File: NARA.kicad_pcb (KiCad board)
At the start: 2 copper layers, 42.4 x 93.9 mm, 0 parts

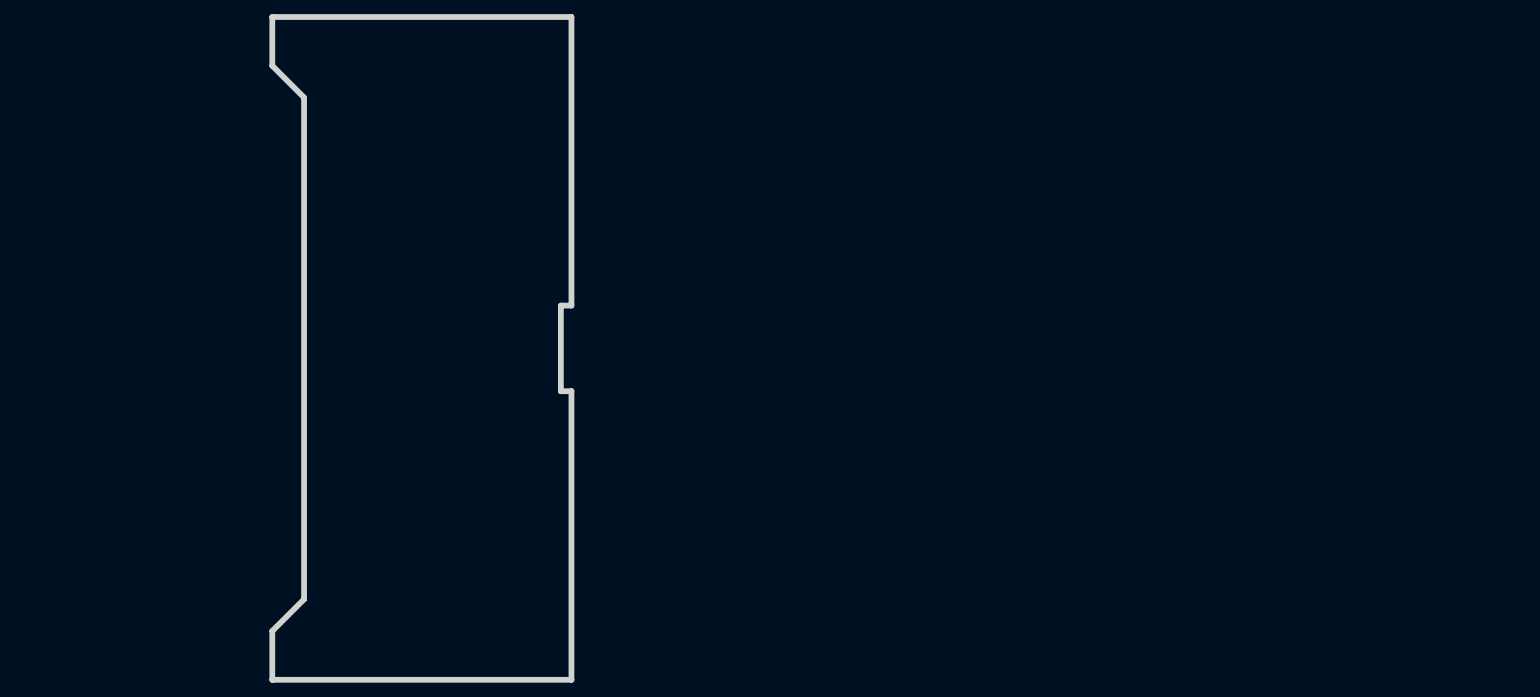
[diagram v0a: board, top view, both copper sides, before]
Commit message: Update footprints, prepare to place composants
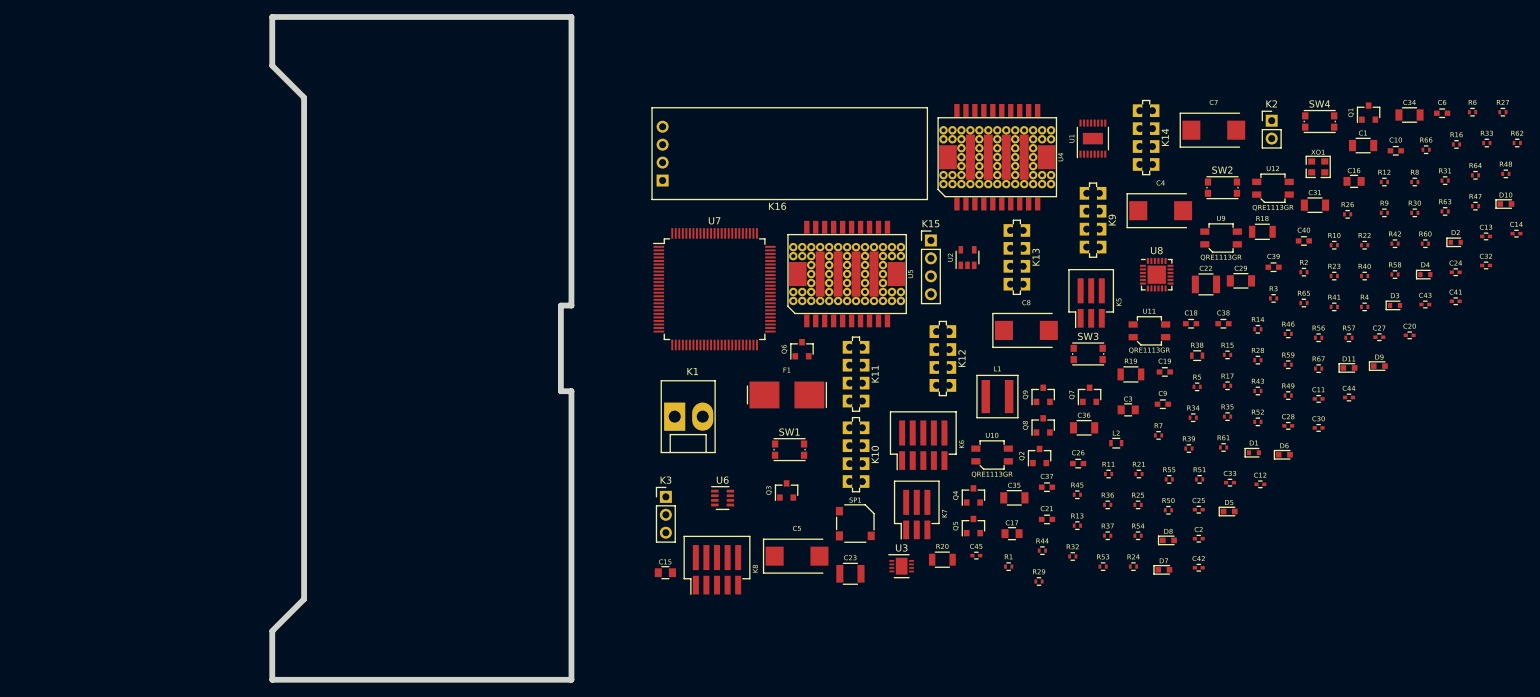
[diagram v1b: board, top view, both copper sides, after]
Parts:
- added C1: C_0038, DVB_Capacitors_Ceramic:C_1206, F.Cu at (239.6, 69.8)
- added C10: C_0033, DVB_Capacitors_Ceramic:C_0603, F.Cu at (244.2, 70.5)
- added C11: C_0002, DVB_Capacitors_Ceramic:C_0402, F.Cu at (233.3, 105.7)
- added C12: C_0034, DVB_Capacitors_Ceramic:C_0402, F.Cu at (225.0, 117.8)
- added C13: C_0034, DVB_Capacitors_Ceramic:C_0402, F.Cu at (257.0, 82.6)
- added C14: C_0045, DVB_Capacitors_Ceramic:C_0402, F.Cu at (261.3, 82.2)
- added C15: C_0056, DVB_Capacitors_Ceramic:C_0805, F.Cu at (140.7, 130.3)
- added C16: C_0056, DVB_Capacitors_Ceramic:C_0805, F.Cu at (238.3, 74.8)
- added C17: C_0056, DVB_Capacitors_Ceramic:C_0805, F.Cu at (189.8, 124.7)
- added C18: C_220nF, DVB_Capacitors_Ceramic:C_0603, F.Cu at (215.2, 95.0)
- added C19: C_220nF, DVB_Capacitors_Ceramic:C_0603, F.Cu at (211.5, 101.8)
- added C2: C_0001, DVB_Capacitors_Ceramic:C_0402, F.Cu at (216.3, 125.5)
- added C20: C_0001, DVB_Capacitors_Ceramic:C_0402, F.Cu at (246.2, 96.7)
- added C21: C_0033, DVB_Capacitors_Ceramic:C_0603, F.Cu at (194.8, 122.7)
- added C22: C_0040, DVB_Capacitors_Ceramic:C_1210, F.Cu at (217.3, 89.4)
- added C23: C_0040, DVB_Capacitors_Ceramic:C_1210, F.Cu at (166.9, 130.4)
- added C24: C_0002, DVB_Capacitors_Ceramic:C_0402, F.Cu at (252.7, 87.7)
- added C25: C_0001, DVB_Capacitors_Ceramic:C_0402, F.Cu at (216.3, 121.3)
- added C26: C_0037, DVB_Capacitors_Ceramic:C_0603, F.Cu at (199.2, 114.8)
- added C27: C_0043, DVB_Capacitors_Ceramic:C_0402, F.Cu at (241.9, 96.9)
- added C28: C_0002, DVB_Capacitors_Ceramic:C_0402, F.Cu at (229.0, 109.5)
- added C29: C_0007, DVB_Capacitors_Ceramic:C_1206, F.Cu at (222.2, 88.9)
- added C3: C_0056, DVB_Capacitors_Ceramic:C_0805, F.Cu at (206.3, 107.2)
- added C30: C_0045, DVB_Capacitors_Ceramic:C_0402, F.Cu at (233.3, 109.8)
- added C31: C_0007, DVB_Capacitors_Ceramic:C_1206, F.Cu at (232.7, 78.2)
- added C32: C_0043, DVB_Capacitors_Ceramic:C_0402, F.Cu at (257.0, 86.8)
- added C33: C_0045, DVB_Capacitors_Ceramic:C_0402, F.Cu at (220.7, 117.5)
- added C34: C_0007, DVB_Capacitors_Ceramic:C_1206, F.Cu at (246.1, 65.4)
- added C35: C_0007, DVB_Capacitors_Ceramic:C_1206, F.Cu at (190.2, 119.7)
- added C36: C_0007, DVB_Capacitors_Ceramic:C_1206, F.Cu at (200.0, 109.7)
- added C37: C_0037, DVB_Capacitors_Ceramic:C_0603, F.Cu at (194.8, 118.2)
- added C38: C_0037, DVB_Capacitors_Ceramic:C_0603, F.Cu at (219.8, 95.0)
- added C39: C_0037, DVB_Capacitors_Ceramic:C_0603, F.Cu at (226.9, 87.0)
- added C4: C_47uF, DVB_Capacitors_Tantalum:CP_EIA-7343-31, F.Cu at (210.9, 79.0)
- added C40: C_0037, DVB_Capacitors_Ceramic:C_0603, F.Cu at (231.2, 83.3)
- added C41: C_0001, DVB_Capacitors_Ceramic:C_0402, F.Cu at (252.7, 91.8)
- added C42: C_0045, DVB_Capacitors_Ceramic:C_0402, F.Cu at (216.3, 129.6)
- added C43: C_0002, DVB_Capacitors_Ceramic:C_0402, F.Cu at (248.4, 92.3)
- added C44: C_0002, DVB_Capacitors_Ceramic:C_0402, F.Cu at (237.6, 105.5)
- added C45: C_470nF, DVB_Capacitors_Ceramic:C_0402, F.Cu at (184.8, 127.8)
- added C5: C_47uF, DVB_Capacitors_Tantalum:CP_EIA-7343-31, F.Cu at (159.4, 127.9)
- added C6: C_0037, DVB_Capacitors_Ceramic:C_0603, F.Cu at (250.8, 65.2)
- added C7: C_47uF, DVB_Capacitors_Tantalum:CP_EIA-7343-31, F.Cu at (218.4, 67.6)
- added C8: C_47uF, DVB_Capacitors_Tantalum:CP_EIA-7343-31, F.Cu at (191.9, 96.0)
- added C9: C_0033, DVB_Capacitors_Ceramic:C_0603, F.Cu at (211.2, 106.4)
- added D1: D_0022, DVB_Diodes:D_SOD-523, F.Cu at (224.1, 113.3)
- added D10: D_0001, DVB_LED:LED_0603-red, F.Cu at (259.8, 78.1)
- added D11: D_0001, DVB_LED:LED_0603-red, F.Cu at (237.6, 101.3)
- added D2: D_0022, DVB_Diodes:D_SOD-523, F.Cu at (252.7, 83.5)
- added D3: D_0022, DVB_Diodes:D_SOD-523, F.Cu at (244.1, 92.4)
- added D4: D_0022, DVB_Diodes:D_SOD-523, F.Cu at (248.4, 88.0)
- added D5: D_0001, DVB_LED:LED_0603-red, F.Cu at (220.6, 121.6)
- added D6: D_0001, DVB_LED:LED_0603-red, F.Cu at (228.4, 113.6)
- added D7: D_0001, DVB_LED:LED_0603-red, F.Cu at (211.3, 129.9)
- added D8: D_0001, DVB_LED:LED_0603-red, F.Cu at (212.0, 125.7)
- added D9: D_0001, DVB_LED:LED_0603-red, F.Cu at (241.9, 101.0)
- added F1: F_001, DVB_F:F-OMNI-BLOCK, F.Cu at (157.9, 105.1)
- added K1: K_KK-41791-02, Connectors_Molex:Molex_KK-41791-02_02x3.96mm_Straight, F.Cu at (142.1, 108.2)
- added K10: TOF_LD, NARA_Lib:GYVL53L0X, F.Cu at (167.7, 113.6)
- added K11: TOF_LS, NARA_Lib:GYVL53L0X, F.Cu at (167.7, 102.2)
- added K12: TOF_LR, NARA_Lib:GYVL53L0X, F.Cu at (180.0, 99.9)
- added K13: TOF_RD, NARA_Lib:GYVL53L0X, F.Cu at (190.5, 85.6)
- added K14: TOF_RS, NARA_Lib:GYVL53L0X, F.Cu at (208.8, 68.6)
- added K15: UART, Pin_Headers:Pin_Header_Straight_1x04_Pitch2.54mm, F.Cu at (178.3, 83.2)
- added K16: OLED_128x32, NARA_Lib:OLED_128x32, F.Cu at (156.6, 69.4)
- added K2: PW_MOT, Pin_Headers:Pin_Header_Straight_1x02_Pitch2.54mm, F.Cu at (226.6, 66.2)
- added K3: PROG, Pin_Headers:Pin_Header_Straight_1x03_Pitch2.54mm, F.Cu at (140.8, 119.5)
- added K5: K_PicoSPOX-3, NARA_Lib:K_PicoSPOX-3, F.Cu at (201.0, 90.6)
- added K6: K_0002, DVB_Connectors:K_PicoSPOX-5, F.Cu at (177.3, 110.7)
- added K7: K_PicoSPOX-3, NARA_Lib:K_PicoSPOX-3, F.Cu at (176.3, 120.6)
- added K8: K_0002, DVB_Connectors:K_PicoSPOX-5, F.Cu at (148.0, 128.4)
- added K9: TOF_LF, NARA_Lib:GYVL53L0X, F.Cu at (201.3, 80.3)
- added L1: L_0002, DVB_Inductors:L_5030-Coilcraft, F.Cu at (187.8, 105.3)
- added L2: L_0010, DVB_Inductors:L_0603, F.Cu at (204.6, 111.9)
- added Q1: Q_0004, DVB_SOT:SOT_23, F.Cu at (240.3, 65.1)
- added Q2: Q_0007, DVB_SOT:SOT_23, F.Cu at (193.7, 113.7)
- added Q3: Q_0007, DVB_SOT:SOT_23, F.Cu at (157.9, 118.6)
- added Q4: Q_0007, DVB_SOT:SOT_23, F.Cu at (184.4, 119.3)
- added Q5: Q_0007, DVB_SOT:SOT_23, F.Cu at (184.4, 123.7)
- added Q6: Q_0007, DVB_SOT:SOT_23, F.Cu at (160.1, 98.6)
- added Q7: Q_0007, DVB_SOT:SOT_23, F.Cu at (200.8, 105.1)
- added Q8: Q_0004, DVB_SOT:SOT_23, F.Cu at (194.2, 109.4)
- added Q9: Q_0004, DVB_SOT:SOT_23, F.Cu at (194.2, 105.1)
- added R1: R_0002, DVB_Resistors:R_0402, F.Cu at (189.4, 129.4)
- added R10: R_0002, DVB_Resistors:R_0402, F.Cu at (235.5, 83.9)
- added R11: R_0111, DVB_Resistors:R_0402, F.Cu at (203.5, 116.3)
- added R12: R_0002, DVB_Resistors:R_0402, F.Cu at (242.6, 74.9)
- added R13: R_0002, DVB_Resistors:R_0402, F.Cu at (199.1, 123.6)
- added R14: R_0111, DVB_Resistors:R_0402, F.Cu at (224.7, 95.8)
- added R15: R_0002, DVB_Resistors:R_0402, F.Cu at (220.4, 99.4)
- added R16: R_0002, DVB_Resistors:R_0402, F.Cu at (252.8, 69.6)
- added R17: R_0030, DVB_Resistors:R_0402, F.Cu at (220.4, 103.8)
- added R18: R_0088, DVB_Resistors:R_1206, F.Cu at (225.3, 82.0)
- added R19: R_0093, DVB_Resistors:R_1206, F.Cu at (206.7, 102.2)
- added R2: R_0002, DVB_Resistors:R_0402, F.Cu at (231.2, 87.7)
- added R20: R_0093, DVB_Resistors:R_1206, F.Cu at (180.0, 128.4)
- added R21: R_0015, DVB_Resistors:R_0402, F.Cu at (207.8, 116.3)
- added R22: R_0015, DVB_Resistors:R_0402, F.Cu at (239.8, 83.9)
- added R23: R_0118, DVB_Resistors:R_0402, F.Cu at (235.5, 88.3)
- added R24: R_0015, DVB_Resistors:R_0402, F.Cu at (207.0, 129.4)
- added R25: R_0104, DVB_Resistors:R_0402, F.Cu at (207.7, 120.7)
- added R26: R_0104, DVB_Resistors:R_0402, F.Cu at (237.4, 79.5)
- added R27: R_0104, DVB_Resistors:R_0402, F.Cu at (259.4, 65.0)
- added R28: R_0104, DVB_Resistors:R_0402, F.Cu at (224.7, 100.2)
- added R29: R_0105, DVB_Resistors:R_0402, F.Cu at (193.7, 131.5)
- added R3: R_0002, DVB_Resistors:R_0402, F.Cu at (226.9, 91.4)
- added R30: R_0105, DVB_Resistors:R_0402, F.Cu at (246.9, 79.3)
- added R31: R_0015, DVB_Resistors:R_0402, F.Cu at (251.2, 74.7)
- added R32: R_0015, DVB_Resistors:R_0402, F.Cu at (198.4, 128.0)
- added R33: R_0015, DVB_Resistors:R_0402, F.Cu at (257.1, 69.4)
- added R34: R_0015, DVB_Resistors:R_0402, F.Cu at (215.5, 108.3)
- added R35: R_0015, DVB_Resistors:R_0402, F.Cu at (220.4, 108.2)
- added R36: R_0015, DVB_Resistors:R_0402, F.Cu at (203.4, 120.7)
- added R37: R_0002, DVB_Resistors:R_0402, F.Cu at (203.4, 125.0)
- added R38: R_0076, DVB_Resistors:R_0603, F.Cu at (216.1, 99.5)
- added R39: R_0002, DVB_Resistors:R_0402, F.Cu at (214.9, 112.7)
- added R4: R_0002, DVB_Resistors:R_0402, F.Cu at (239.8, 92.6)
- added R40: R_0002, DVB_Resistors:R_0402, F.Cu at (239.8, 88.3)
- added R41: R_0002, DVB_Resistors:R_0402, F.Cu at (235.5, 92.6)
- added R42: R_0002, DVB_Resistors:R_0402, F.Cu at (244.1, 83.7)
- added R43: R_0002, DVB_Resistors:R_0402, F.Cu at (224.7, 104.5)
- added R44: R_0002, DVB_Resistors:R_0402, F.Cu at (194.1, 127.1)
- added R45: R_0002, DVB_Resistors:R_0402, F.Cu at (199.1, 119.2)
- added R46: R_0002, DVB_Resistors:R_0402, F.Cu at (229.0, 96.4)
- added R47: R_0033, DVB_Resistors:R_0402, F.Cu at (255.5, 78.4)
- added R48: R_0033, DVB_Resistors:R_0402, F.Cu at (259.8, 73.8)
- added R49: R_0033, DVB_Resistors:R_0402, F.Cu at (229.0, 105.2)
- added R5: R_0002, DVB_Resistors:R_0402, F.Cu at (216.1, 103.9)
- added R50: R_0033, DVB_Resistors:R_0402, F.Cu at (212.0, 121.4)
- added R51: R_0003, DVB_Resistors:R_0402, F.Cu at (216.4, 117.1)
- added R52: R_0003, DVB_Resistors:R_0402, F.Cu at (224.7, 108.9)
- added R53: R_0105, DVB_Resistors:R_0402, F.Cu at (202.7, 129.4)
- added R54: R_0105, DVB_Resistors:R_0402, F.Cu at (207.7, 125.0)
- added R55: R_0105, DVB_Resistors:R_0402, F.Cu at (212.1, 117.1)
- added R56: R_0105, DVB_Resistors:R_0402, F.Cu at (233.3, 97.0)
- added R57: R_0104, DVB_Resistors:R_0402, F.Cu at (237.6, 97.0)
- added R58: R_0033, DVB_Resistors:R_0402, F.Cu at (244.1, 88.0)
- added R59: R_0105, DVB_Resistors:R_0402, F.Cu at (229.0, 100.8)
- added R6: R_0002, DVB_Resistors:R_0402, F.Cu at (255.1, 65.0)
- added R60: R_0105, DVB_Resistors:R_0402, F.Cu at (248.4, 83.7)
- added R61: R_0033, DVB_Resistors:R_0402, F.Cu at (219.8, 112.5)
- added R62: R_0111, DVB_Resistors:R_0402, F.Cu at (261.4, 69.4)
- added R63: R_0111, DVB_Resistors:R_0402, F.Cu at (251.2, 79.1)
- added R64: R_0111, DVB_Resistors:R_0402, F.Cu at (255.5, 74.0)
- added R65: R_0111, DVB_Resistors:R_0402, F.Cu at (231.2, 92.1)
- added R66: R_0111, DVB_Resistors:R_0402, F.Cu at (248.5, 70.4)
- added R67: R_0111, DVB_Resistors:R_0402, F.Cu at (233.3, 101.4)
- added R7: R_0111, DVB_Resistors:R_0402, F.Cu at (210.6, 110.8)
- added R8: R_0002, DVB_Resistors:R_0402, F.Cu at (246.9, 74.9)
- added R9: R_0002, DVB_Resistors:R_0402, F.Cu at (242.6, 79.3)
- added SP1: SP_0001, DVB_Buzzers:SP_KSSG-5x5x3, F.Cu at (167.6, 123.3)
- added SW1: SW_KMR2, Buttons_Switches_SMD:SW_SPST_KMR2, F.Cu at (158.3, 112.8)
- added SW2: SW_KMR2, Buttons_Switches_SMD:SW_SPST_KMR2, F.Cu at (219.6, 75.7)
- added SW3: SW_KMR2, Buttons_Switches_SMD:SW_SPST_KMR2, F.Cu at (200.6, 99.3)
- added SW4: SW_KMR2, Buttons_Switches_SMD:SW_SPST_KMR2, F.Cu at (233.4, 66.4)
- added U1: U_LT8610ABIMSE-3.3, DVB_SSOP:MSOP_16-1EP_3x4_P0.5, F.Cu at (201.3, 68.8)
- added U10: QRE1113GR, NARA_Lib:QRE1113GR, F.Cu at (187.0, 113.6)
- added U11: QRE1113GR, NARA_Lib:QRE1113GR, F.Cu at (209.3, 96.0)
- added U12: QRE1113GR, NARA_Lib:QRE1113GR, F.Cu at (226.8, 75.8)
- added U2: U_AP2204K-5.0TRG1, DVB_SOT:SOT_23-5, F.Cu at (183.5, 85.6)
- added U3: LTC2944, Housings_DFN_QFN:DFN-8-1EP_3x3mm_Pitch0.5mm, F.Cu at (174.2, 129.3)
- added U4: L6234, NARA_Lib:PowerSO-20, F.Cu at (187.7, 71.4)
- added U5: L6234, NARA_Lib:PowerSO-20, F.Cu at (166.5, 88.0)
- added U6: LTC2955TS8-1, TO_SOT_Packages_SMD:SOT-23-8, F.Cu at (148.8, 119.7)
- added U7: STM32H743VITx, Housings_QFP:LQFP-100_14x14mm_Pitch0.5mm, F.Cu at (147.7, 90.1)
- added U8: ICM-20689, Housings_DFN_QFN:QFN-24-1EP_4x4mm_Pitch0.5mm, F.Cu at (210.3, 88.1)
- added U9: QRE1113GR, NARA_Lib:QRE1113GR, F.Cu at (219.4, 82.9)
- added XO1: XO_8Z-16, DVB_Clock:XO_8Z, F.Cu at (233.2, 72.8)

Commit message: First components placement, Autoroute in progress
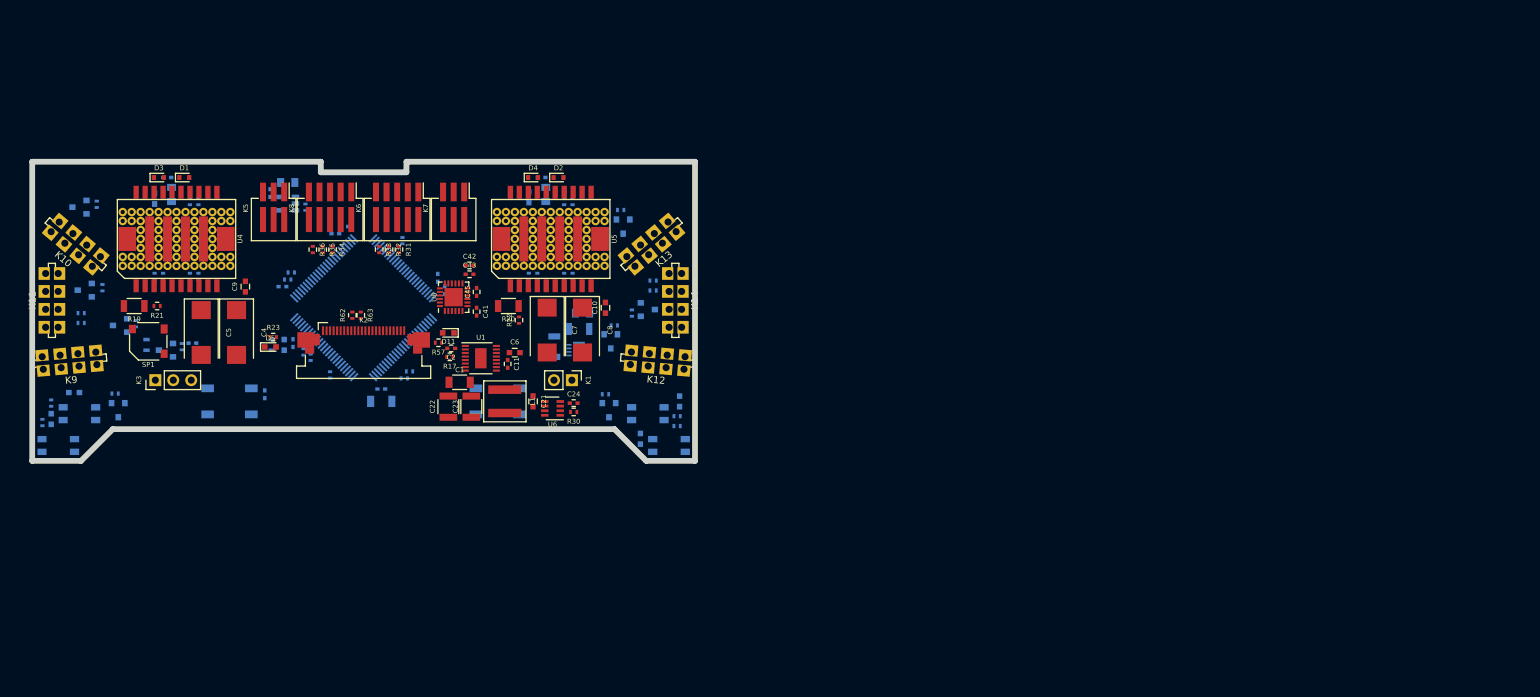
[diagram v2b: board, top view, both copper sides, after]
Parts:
- removed C20: C_0001, DVB_Capacitors_Ceramic:C_0402
- removed C27, C32: C_0043, DVB_Capacitors_Ceramic:C_0402
- removed D10, D6, D7, D8, D9: D_0001, DVB_LED:LED_0603-red
- removed K15: UART, Pin_Headers:Pin_Header_Straight_1x04_Pitch2.54mm
- removed K16: OLED_128x32, NARA_Lib:OLED_128x32
- removed R24: R_0015, DVB_Resistors:R_0402
- removed R25, R26, R27, R28: R_0104, DVB_Resistors:R_0402
- removed R51, R52: R_0003, DVB_Resistors:R_0402
- removed R58, R61: R_0033, DVB_Resistors:R_0402
- removed R59, R60: R_0105, DVB_Resistors:R_0402
- removed SW3, SW4: SW_KMR2, Buttons_Switches_SMD:SW_SPST_KMR2
- removed XO1: XO_8Z-16, DVB_Clock:XO_8Z
- C12, C13, C14, C15, C16, C17, C18, C19, C25, C26, C28, C29, C3, C30, C33, C37, C38, C39, C40, C44, L2, Q1, Q2, Q3, Q4, Q5, Q6, Q7, Q8, Q9, R1, R10, R11, R12, R13, R14, R15, R16, R18, R2, R29, R3, R37, R38, R39, R4, R40, R41, R42, R43, R44, R45, R46, R47, R48, R49, R5, R50, R53, R54, R55, R56, R6, R64, R65, R66, R67, R7, R8, R9, U10, U11, U12, U2, U9: moved to B.Cu
- C31, C34, C35, C36: value C_0007 -> C_0002; footprint DVB_Capacitors_Ceramic:C_1206 -> DVB_Capacitors_Ceramic:C_0402; moved to B.Cu
- F1: value F_001 -> FUSE; footprint DVB_F:F-OMNI-BLOCK -> DVB_F:F_1206; moved to B.Cu
- K1: value K_KK-41791-02 -> BATT; footprint Connectors_Molex:Molex_KK-41791-02_02x3.96mm_Straight -> DVB_Connectors:Pin_Header_Straight_1x02_Pitch2.54mm
- K12: value TOF_LR -> TOF_RF
- K2: value PW_MOT -> K_FPC_52435-2471; footprint Pin_Headers:Pin_Header_Straight_1x02_Pitch2.54mm -> DVB_Connectors:K_FPC_52435-2471
- K3: footprint Pin_Headers:Pin_Header_Straight_1x03_Pitch2.54mm -> DVB_Connectors:Pin_Header_Straight_1x03_Pitch2.54mm
- SW1, SW2: value SW_KMR2 -> SW_SKQG; footprint Buttons_Switches_SMD:SW_SPST_KMR2 -> DVB_Buttons:SPST_SKQG; moved to B.Cu
- U3: footprint Housings_DFN_QFN:DFN-8-1EP_3x3mm_Pitch0.5mm -> DVB_QFN_DFN:DFN_8-1EP_3x3mm_P0.5mm; moved to B.Cu
- U6: footprint TO_SOT_Packages_SMD:SOT-23-8 -> DVB_SOT:SOT_23-8
- U7: footprint Housings_QFP:LQFP-100_14x14mm_Pitch0.5mm -> DVB_QFP:LQFP-100_14x14mm_Pitch0.5mm; moved to B.Cu
- U8: footprint Housings_DFN_QFN:QFN-24-1EP_4x4mm_Pitch0.5mm -> DVB_QFN_DFN:QFN-24-1EP_4x4mm_Pitch0.5mm
- moved R48 208.6 mm to (53.8, 106.2), turned to 90 degrees
- moved R47 205.3 mm to (52.5, 109.0), turned to 270 degrees
- moved R64 198.6 mm to (58.0, 94.9)
- moved R40 179.9 mm to (60.2, 78.1), turned to 90 degrees
- moved C14 176.6 mm to (84.8, 76.5), turned to 90 degrees
- moved D3 176.0 mm to (69.0, 74.3)
- moved R12 174.7 mm to (68.4, 88.3), turned to 270 degrees
- moved R41 174.5 mm to (61.0, 89.9), turned to 90 degrees
- moved Q1 173.6 mm to (70.0, 98.8), turned to 270 degrees
- moved R65 173.2 mm to (58.0, 93.5), turned to 180 degrees
- moved R9 168.2 mm to (74.6, 88.3), turned to 270 degrees
- moved U9 167.3 mm to (54.8, 112.2)
- moved R62 166.8 mm to (96.4, 93.8), turned to 90 degrees
- moved C38 163.1 mm to (57.0, 104.8), turned to 180 degrees
- moved C12 160.8 mm to (70.2, 74.3)
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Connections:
- C10 pad 1: +HBAT -> +BATT
- C21 pad 1: +BATT -> GND
- C21 pad 2: GND -> +BATT
- C4 pad 1: +HBAT -> +BATT
- C5 pad 1: +HBAT -> +BATT
- C7 pad 1: +HBAT -> +BATT
- C8 pad 1: +HBAT -> +BATT
- C9 pad 1: +HBAT -> +BATT
- D1 pad 2: +HBAT -> +BATT
- D2 pad 2: +HBAT -> +BATT
- K2 pad 1: +BATT -> GND
- K2 pad 2: +HBAT -> /SW_PW
- SW1 pad 1: GND -> /SW_PW
- SW1 pad 2: Net-(SW1-Pad2) -> GND
- U4 pad 12: +HBAT -> +BATT
- U4 pad 9: +HBAT -> +BATT
- U5 pad 12: +HBAT -> +BATT
- U5 pad 9: +HBAT -> +BATT
- U6 pad 5: Net-(SW1-Pad2) -> /SW_PW
- U7 pad 12: Net-(C27-Pad2) -> (no net)
- U7 pad 13: Net-(C32-Pad1) -> (no net)
- U7 pad 17: (no net) -> /EXT_ADC1
- U7 pad 18: (no net) -> /EXT_ADC2
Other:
- board size 42.4 x 93.9 mm -> 93.9 x 42.4 mm
- net class Default: clearance 0.2 -> 0.13; trace_width 0.25 -> 0.13; via_drill 0.4 -> 0.2
- rule trace_clearance: 0.2 -> 0.13
- rule trace_min: 0.2 -> 0.125
- rule via_min_drill: 0.3 -> 0.2
- rule via_min_size: 0.4 -> 0.6

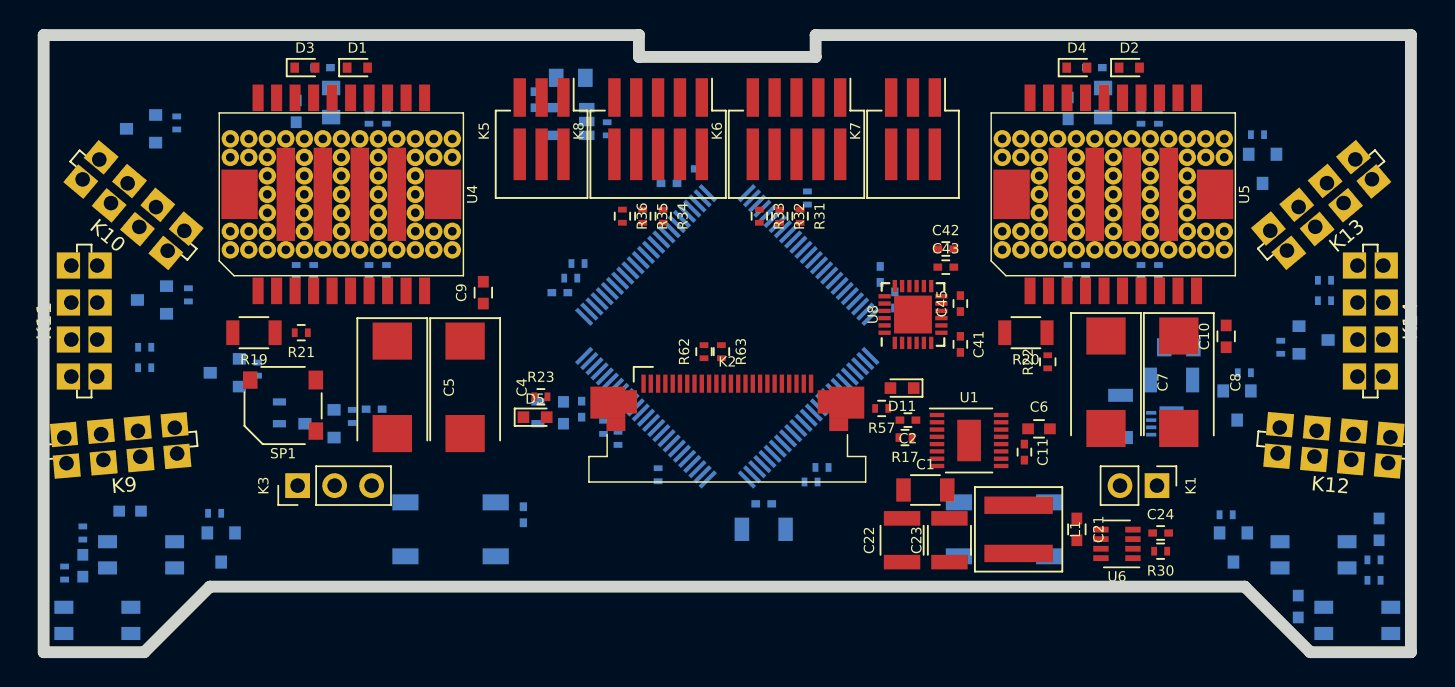
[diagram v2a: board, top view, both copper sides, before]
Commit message: Add GND and PWR layer
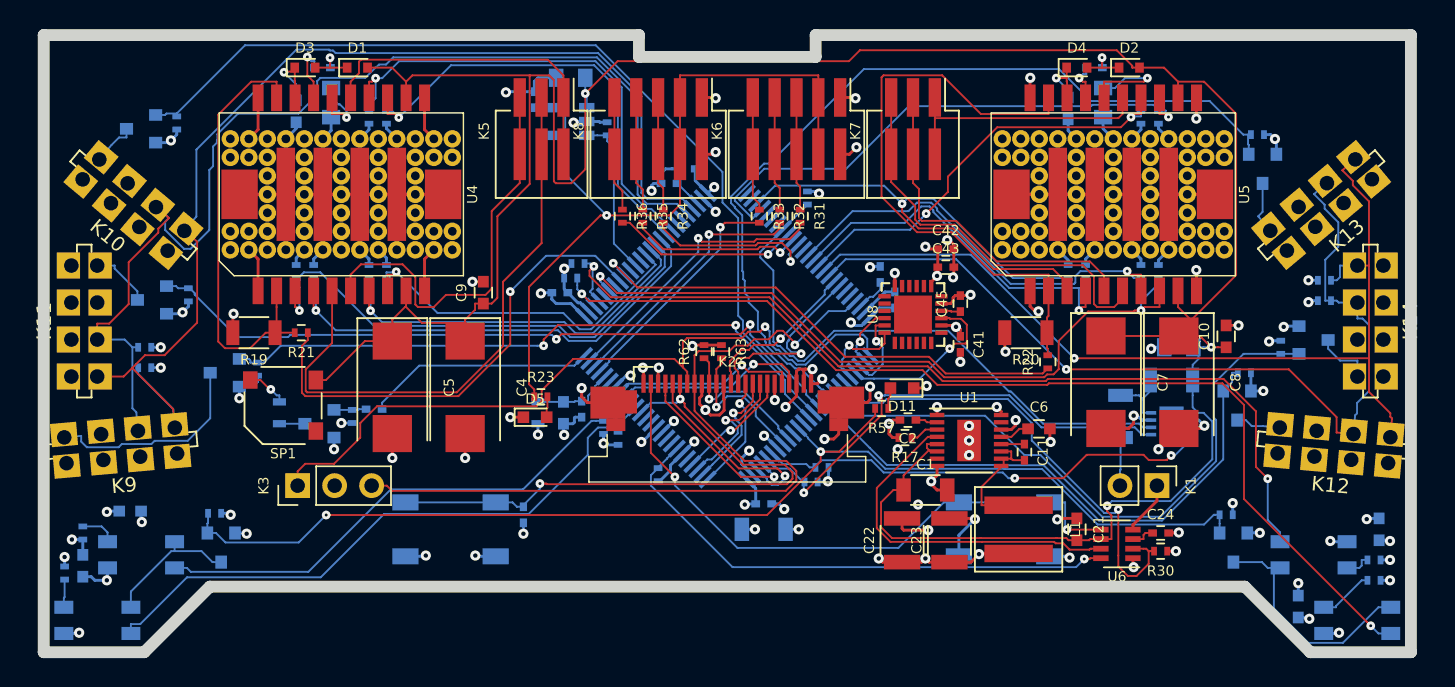
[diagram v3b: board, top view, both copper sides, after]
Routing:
- net GND: track 0.00 -> 767.1 mm, vias 0 -> 76
- net +3.3V: track 0.00 -> 323.2 mm, vias 0 -> 42
- net +BATT: track 0.00 -> 189.7 mm, vias 0 -> 3
- net /LINE_EN: track 0.00 -> 85.2 mm, vias 0 -> 2
- net /TOF_L_SCL: track 0.00 -> 77.3 mm
- net /TOF_L_SDA: track 0.00 -> 76.7 mm
- net /LINE_ADC_R1: track 0.00 -> 71.5 mm, vias 0 -> 2
- net /TOF_R_SDA: track 0.00 -> 65.2 mm, vias 0 -> 1
- net /TOF_EN_LD: track 0.00 -> 63.8 mm
- net /TOF_R_SCL: track 0.00 -> 63.8 mm, vias 0 -> 1
- net /LINE_ADC_R2: track 0.00 -> 63.6 mm, vias 0 -> 2
- net /TOF_EN_RD: track 0.00 -> 59.6 mm
- net /SWDIO: track 0.00 -> 56.2 mm, vias 0 -> 1
- net +5V: track 0.00 -> 54.9 mm, vias 0 -> 1
- net /SWCLK: track 0.00 -> 51.8 mm, vias 0 -> 1
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- added copper zone on GND.Cu, net GND
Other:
- copper layers 2 -> 4
- net class Default: clearance 0.13 -> 0.127
- net class GND added: clearance 0.127, trace_width 0.2, via_dia 0.6, via_drill 0.2
- net class PWR added: clearance 0.127, trace_width 0.2, via_dia 0.7, via_drill 0.3
- rule trace_clearance: 0.13 -> 0.127
